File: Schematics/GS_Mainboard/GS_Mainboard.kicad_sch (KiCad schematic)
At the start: 0 parts

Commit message: Completed schematic
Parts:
- added C1: 10n, Capacitor_SMD:C_0603_1608Metric, symbol Device:C
- added C10, C32, C33, C5, C6, C9: 100n, Capacitor_SMD:C_0402_1005Metric, symbol Device:C
- added C11: 33pF, Capacitor_SMD:C_0402_1005Metric, symbol Device:C
- added C11 (x4): 47uF, Capacitor_SMD:C_0805_2012Metric, symbol Device:C
- added C11, C17: 22uF, Capacitor_SMD:C_0805_2012Metric, symbol Device:C
- added C11, C4 (x2), C7 (x2): 100nF, Capacitor_SMD:C_0603_1608Metric, symbol Device:C
- added C12: 10uF, Capacitor_SMD:C_0603_1608Metric, symbol Device:C
- added C13: 22uF, Capacitor_SMD:C_0603_1608Metric, symbol Device:C
- added C14: 2000uF, 25V, Capacitor_THT:CP_Radial_D12.5mm_P5.00mm, symbol Device:C_Polarized
- added C14: 1000uF, 25V, Capacitor_THT:CP_Radial_D10.0mm_P5.00mm, symbol Device:C_Polarized
- added C14: 100uF, Capacitor_SMD:CP_Elec_6.3x5.9, symbol Device:C_Polarized
- added C2 (x2): 2.2uF, Capacitor_SMD:C_0603_1608Metric_Pad1.08x0.95mm_HandSolder, symbol Device:C
- added C2 (x2): 4.7uF, Capacitor_SMD:C_0805_2012Metric, symbol Device:C
- added C2: 10uF, Capacitor_SMD:CP_Elec_4x5.4, symbol Device:C_Polarized
- added C29, C30, C34, C35, C36, C37, C38: 1uF, Capacitor_SMD:C_0603_1608Metric, symbol Device:C
- added C4, C8: 1uF, Capacitor_SMD:C_0805_2012Metric, symbol Device:C_Polarized
- added C46: 0.1u, Capacitor_SMD:C_0603_1608Metric, symbol Device:C
- added D1: DB_LED (YLW), LED_SMD:LED_0603_1608Metric, symbol Device:LED
- added D1: 12V PWR (GRN), LED_SMD:LED_0805_2012Metric, symbol Device:LED
- added D1: 5.0V PWR (GRN), LED_SMD:LED_0805_2012Metric, symbol Device:LED
- added D1: 3.3V PWR (GRN), LED_SMD:LED_0805_2012Metric, symbol Device:LED
- added D10, D11: 15Vz, Diode_SMD:D_SOD-123, symbol Device:D_Zener
- added D5, D6, D7, D8, D9: WS2812B, LED_SMD:LED_WS2812B_PLCC4_5.0x5.0mm_P3.2mm, symbol LED:WS2812B
- added FB1: 100R, Resistor_SMD:R_0805_2012Metric, symbol Device:FerriteBead
- added H1, H2, H3, H4, H5, H6: MountingHole, MountingHole:MountingHole_3.2mm_M3_ISO14580_Pad, symbol Mechanical:MountingHole
- added J1: SWD Header, footprints:PinHeader_1x6_P2.54mm_Drill1.02mm, symbol Connector:Conn_01x06_Pin
- added J10: GPIO, footprints:PinHeader_1x6_P2.54mm_Drill1.02mm, symbol Connector:Conn_01x06_Pin
- added J11: RTX_PWR, TerminalBlock:TerminalBlock_bornier-2_P5.08mm, symbol Connector:Screw_Terminal_01x02
- added J12: SRC_IND, TerminalBlock_TE-Connectivity:TerminalBlock_TE_282834-3_1x03_P2.54mm_Horizontal, symbol Connector:Screw_Terminal_01x03
- added J13: BATT1, TerminalBlock:TerminalBlock_bornier-2_P5.08mm, symbol Connector:Screw_Terminal_01x02
- added J14: BATT2, TerminalBlock:TerminalBlock_bornier-2_P5.08mm, symbol Connector:Screw_Terminal_01x02
- added J15: SWITCH, TerminalBlock:TerminalBlock_bornier-2_P5.08mm, symbol Connector:Screw_Terminal_01x02
- added J16: BUTTS, TerminalBlock:TerminalBlock_bornier-4_P5.08mm, symbol Connector:Screw_Terminal_01x04
- added J17: POWER, TerminalBlock:TerminalBlock_bornier-4_P5.08mm, symbol Connector:Screw_Terminal_01x04
- added J2: RASPI, footprints:PinHeader_1x6_P2.54mm_Drill1.02mm, symbol Connector:Conn_01x06_Pin
- added J3, J5: RGB_OUT, footprints:PinHeader_1x3_P2.54mm_Drill1.02mm, symbol dk_Rectangular-Connectors-Headers-Male-Pins:640456-3
- added J4: RGB_IN, footprints:PinHeader_1x3_P2.54mm_Drill1.02mm, symbol dk_Rectangular-Connectors-Headers-Male-Pins:640456-3
- added J6: FAN1, footprints:PinHeader_1x3_P2.54mm_Drill1.02mm, symbol dk_Rectangular-Connectors-Headers-Male-Pins:640456-3
- added J7: FAN2, footprints:PinHeader_1x3_P2.54mm_Drill1.02mm, symbol dk_Rectangular-Connectors-Headers-Male-Pins:640456-3
- added J8: RGB12V, TerminalBlock:TerminalBlock_bornier-4_P5.08mm, symbol Connector:Screw_Terminal_01x04
- added L2: 12uH, Inductor_SMD:L_Bourns_SRR1260, symbol Device:L
- added L2: 4.7uH, Inductor_SMD:L_Bourns_SRN8040TA, symbol Device:L
- added Q1 (x3): AO4447A, Package_SO:SOIC-8_3.9x4.9mm_P1.27mm, symbol Transistor_FET:IRF7404
- added Q1, Q10, Q11, Q2, Q3, Q4, Q5: AO3400A, Package_TO_SOT_SMD:SOT-23, symbol Transistor_FET:AO3400A
- added Q12, Q9: AO4406A, Package_SO:SOIC-8_3.9x4.9mm_P1.27mm, symbol Transistor_FET:IRF7403
- added R1, R17, R26, R35, R37, R38, R41, R44, R45, R46: 10k, Resistor_SMD:R_0603_1608Metric, symbol Device:R
- added R10, R7: 68k, Resistor_SMD:R_0603_1608Metric, symbol Device:R
- added R10: 33k, Resistor_SMD:R_0603_1608Metric, symbol Device:R
- added R10: 1k, Resistor_SMD:R_0603_1608Metric, symbol Device:R
- added R11: 6.2k, Resistor_SMD:R_0603_1608Metric, symbol Device:R
- added R11: 3.6k, Resistor_SMD:R_0603_1608Metric, symbol Device:R
- added R13, R14: 30k, Resistor_SMD:R_0603_1608Metric, symbol Device:R
- added R15: 47k, Resistor_SMD:R_0603_1608Metric, symbol Device:R
- added R16: 13k, Resistor_SMD:R_0603_1608Metric, symbol Device:R
- added R18, R2, R21, R23, R25, R29, R3, R40, R43: 100k, Resistor_SMD:R_0603_1608Metric, symbol Device:R
- added R19, R20, R22, R24, R27, R39, R42: 510R, Resistor_SMD:R_0603_1608Metric, symbol Device:R
- added R28: 100k, Resistor_SMD:R_0402_1005Metric, symbol Device:R
- added R30, R31: 1k, Resistor_THT:R_Axial_DIN0204_L3.6mm_D1.6mm_P5.08mm_Horizontal, symbol Device:R
- added R32, R33, R7: 15k, Resistor_SMD:R_0603_1608Metric, symbol Device:R
- added R34, R36: 75k, Resistor_SMD:R_0603_1608Metric, symbol Device:R
- added R4: 680R, Resistor_SMD:R_0603_1608Metric, symbol Device:R
- added R7: 3.3k, Resistor_SMD:R_0603_1608Metric, symbol Device:R
- added SW1: SW_STM_RESET, Button_Switch_SMD:SW_Push_1P1T_XKB_TS-1187A, symbol Switch:SW_Push
- added SW2: SW_STM_BOOT_MODE, Button_Switch_SMD:SW_Push_1P1T_XKB_TS-1187A, symbol Switch:SW_Push
- added TH1: 10k, Resistor_SMD:R_0603_1608Metric_Pad0.98x0.95mm_HandSolder, symbol Device:Thermistor_NTC
- added TP11: CURR, TestPoint:TestPoint_Pad_1.5x1.5mm, symbol Connector:TestPoint
- added TP5: 5VS, TestPoint:TestPoint_Pad_2.0x2.0mm, symbol Connector:TestPoint
- added TP5: 12VS, TestPoint:TestPoint_Pad_2.0x2.0mm, symbol Connector:TestPoint
- added TP5 (x2): B1_S, TestPoint:TestPoint_Pad_2.0x2.0mm, symbol Connector:TestPoint
- added U2: LMR51430XDDCR, Package_TO_SOT_SMD:SOT-23-6_Handsoldering, symbol QRET_Buck_PSU-symbols:LMR51430XDDCR
- added U3: K7805JT-500R3, footprints:K7805JT_500R3, symbol K7805JT_500R3:K7805JT-500R3
- added U4: 296-LMR51450FNDRRRCT-ND, footprints:LMR51450SDRRR, symbol LMR51450SDRRR:LMR51450SDRRR
- added U4: STM32F103C8T6, Package_QFP:LQFP-48_7x7mm_P0.5mm, symbol MCU_ST_STM32F1:STM32F103C8Tx
- added U5, U6: LM66100DCKR, footprints:LMR66100_SC-70-6, symbol QRET_Buck_PSU-symbols:LM66100DCKR
- added U7, U8: LM74700QDDFRQ1, footprints:LM74700_SOT-23-THIN_1P6X2P9_TEX-M, symbol LM74700QDDFRQ1:LM74700QDDFRQ1
- added U9: ACS37041KLHBLT-010B3, footprints:APS12628LLHALTBAP_HandSolder, symbol ACS37041KLHBLT-010B3:ACS37041KLHBLT-010B3
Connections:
- new net: D1.2 (A), R4.1
- new net: R10.2, R11.1, U2.4 (FB)
- new net: Q10.3 (D), R38.2, U7.1 (EN)
- new net: Q4.1 (G), R24.2
- new net: J8.2 (Pin_2), Q4.3 (D)
- new net: Q2.1 (G), R20.2
- new net: C11.1, R10.2
- new net: C11.2, R10.2, R11.1, U4.7 (FB)
- new net: J6.1, J7.1, Q1.3 (D)
- new net: C7.1, L2.1, U4.1 (SW), U4.2 (SW__1), U4.3 (SW__2)
- new net: C7.2, U4.4 (BOOT)
- new net: C7.1, L2.1, U2.2 (SW)
- new net: C7.2, U2.6 (CB)
- new net: J12.3 (Pin_3), R31.1
- new net: Q5.1 (G), R27.1
- new net: Q1.4 (G), Q5.3 (D), R28.2
- new net: D1.2 (A), R7.2 (x3)
- new net: J11.2 (Pin_2), Q1.5 (D), Q1.6 (D), Q1.7 (D), Q1.8 (D)
- new net: D10.2 (A), Q1.4 (G), R32.1
- new net: J13.2 (Pin_2), Q1.5 (D), Q1.6 (D), Q1.7 (D), Q1.8 (D)
- new net: D11.2 (A), Q1.4 (G), R33.1
- new net: D7.2 (DOUT), D8.4 (DIN)
- new net: D6.2 (DOUT), D7.4 (DIN)
- new net: Q1.1 (G), R19.2
- new net: Q10.1 (G), R39.2
- new net: J8.4 (Pin_4), Q2.3 (D)
- new net: C38.2, U8.4 (VCAP)
- new net: C35.2, U7.4 (VCAP)
- new net: Q9.4 (G), U7.6 (GATE)
- new net: Q12.4 (G), U8.6 (GATE)
- new net: J13.1 (Pin_1), J14.1 (Pin_1), J15.2 (Pin_2)
- new net: Q11.1 (G), R42.2
- new net: Q11.3 (D), R41.2, U8.1 (EN)
- new net: Q3.1 (G), R22.2
- new net: J14.2 (Pin_2), Q1.5 (D), Q1.6 (D), Q1.7 (D), Q1.8 (D)
- new net: J8.3 (Pin_3), Q3.3 (D)
- new net: C30.2, U6.2 (GND)
- new net: D8.2 (DOUT), D9.4 (DIN)
- new net: J12.2 (Pin_2), R30.1
- new net: D5.2 (DOUT), D6.4 (DIN)
- new net +12V: C11.1, C14.1, C17.1, J17.3 (Pin_3), J6.3, J7.3, J8.1 (Pin_1), L2.2, Q1.1 (S), Q1.2 (S), Q1.3 (S), R10.1, R15.2, R28.1
- new net +3.3V: C10.1, C11.1, C2.1, C5.1, C6.1, C8.1, C9.1, FB1.2, J10.2 (Pin_2), J3.2, R1.2, R17.2, R26.1, R44.2, R45.2, R46.2, R7.1, R7.1, R7.1, SW2.2, U4.1 (VBAT), U4.24 (VDD), U4.36 (VDD), U4.48 (VDD), U5.3 (*CE), U5.6 (VOUT), U6.3 (*CE), U6.6 (VOUT)
- new net +3.3VA: C1.1, C4.1, FB1.1, U4.9 (VDDA)
- new net +5V: C11.1, C11.1, C14.1, J17.4 (Pin_4), J2.1 (Pin_1), J2.2 (Pin_2), L2.2, R10.1, R10.1, R13.2
- new net +BATT: C11.1, C12.1, C14.1, C2.1, C2.1, C4.1, C4.1, J17.2 (Pin_2), U2.3 (VIN), U2.5 (EN), U3.1 (+Vin), U4.10 (VIN), U4.11 (VIN__1), U4.12 (VIN__2), U4.9 (EN), U9.2 (IP-)
- new net 12V_SENSE: R15.1, R16.2, TP5.1, U4.14 (PA4)
- new net 5V_SENSE: R13.1, R14.2, TP5.1, U4.13 (PA3)
- new net BATT1_EN: R30.2, R39.1, R40.2, U4.17 (PA7)
- new net BATT1_RAW: C35.1, C36.1, D10.1 (K), Q1.1 (S), Q1.2 (S), Q1.3 (S), Q9.1 (S), Q9.2 (S), Q9.3 (S), R34.1, R38.1, U7.5 (ANODE)
- new net BATT2_EN: R31.2, R42.1, R43.2, U4.29 (PA8)
- new net BATT2_RAW: C37.1, C38.1, D11.1 (K), Q1.1 (S), Q1.2 (S), Q1.3 (S), Q12.1 (S), Q12.2 (S), Q12.3 (S), R36.1, R41.1, U8.5 (ANODE)
- new net BATT_1_SENSE: C32.1, R34.2, R35.1, TP5.1, U4.10 (PA0)
- new net BATT_2_SENSE: C33.1, R36.2, R37.1, TP5.1, U4.11 (PA1)
- new net BATT_COM: C34.1, Q12.5 (D), Q12.6 (D), Q12.7 (D), Q12.8 (D), Q9.5 (D), Q9.6 (D), Q9.7 (D), Q9.8 (D), U7.8 (CATHODE), U8.8 (CATHODE), U9.1 (IP+)
- new net BOOT0: R2.2, SW2.1, U4.44 (BOOT0)
- new net BOOT1: R3.2, U4.20 (PB2)
- new net BUTT_1: J16.2 (Pin_2), R44.1, U4.46 (PB9)
- new net BUTT_2: J16.3 (Pin_3), R45.1, U4.43 (PB7)
- new net BUTT_3: J16.4 (Pin_4), R46.1, U4.45 (PB8)
- new net CURR_PWR: C46.1, U4.16 (PA6), U9.5 (VDD)
- new net CURR_SENSE: TP11.1, U4.12 (PA2), U9.4 (VOUT)
- new net DB_LED: R4.2, U4.38 (PA15)
- new net FAN_PWM: R18.2, R19.1, U4.19 (PB1)
- new net FAN_TACH: J6.2, R17.1, U4.18 (PB0)
- new net GND: C1.2, C10.2, C11.2, C11.2, C11.2, C11.2, C11.2, C11.2, C12.2, C13.2, C14.2, C14.2, C17.2, C2.2, C2.2, C2.2, C29.2, C32.2, C33.2, C34.2, C36.2, C37.2, C4.2, C4.2, C4.2, C5.2, C6.2, C8.2, C9.2, D1.1 (K), D1.1 (K), D1.1 (K), D1.1 (K), J1.1 (Pin_1), J10.1 (Pin_1), J11.1 (Pin_1), J12.1 (Pin_1), J15.1 (Pin_1), J16.1 (Pin_1), J17.1 (Pin_1), J2.3 (Pin_3), J2.4 (Pin_4), J3.1, Q1.2 (S), Q10.2 (S), Q11.2 (S), Q2.2 (S), Q3.2 (S), Q4.2 (S), Q5.2 (S), R11.2, R11.2, R14.1, R16.1, R18.1, R2.1, R21.1, R23.1, R25.1, R29.1, R3.1, R32.2, R33.2, R35.2, R37.2, R40.1, R43.1, SW1.1, TH1.2, U2.1 (GND), U3.4 (GND), U4.13 (PGND), U4.23 (VSS), U4.35 (VSS), U4.47 (VSS), U4.8 (AGND), U4.8 (VSSA), U5.2 (GND), U5.5 (ST), U6.5 (ST), U7.2 (GND), U8.2 (GND)
- new net GND2: C14.2, C46.2, U9.3 (GND)
- new net GPIO1: J10.4 (Pin_4), U4.25 (PB12)
- new net GPIO2: J10.3 (Pin_3), U4.26 (PB13)
- new net OSC_IN: U4.5 (PD0)
- new net OSC_OUT: U4.6 (PD1)
- new net PSU_TEMP: R26.2, TH1.1, U4.15 (PA5)
- new net RGB12_B: R22.1, R23.2, U4.41 (PB5)
- new net RGB12_G: R20.1, R21.2, U4.40 (PB4)
- new net RGB12_R: R24.1, R25.2, U4.39 (PB3)
- new net RGB_DATA: J3.3, U4.27 (PB14)
- new net RGB_DATA_IN: D5.4 (DIN), J4.3
- new net RGB_DATA_OUT: D9.2 (DOUT), J5.3
- new net RGB_GND: C2.1, C2.1, D5.3 (VSS), D6.3 (VSS), D7.3 (VSS), D8.3 (VSS), D9.3 (VSS), J4.1, J5.1
- new net RGB_V+: C2.2, C2.2, D5.1 (VDD), D6.1 (VDD), D7.1 (VDD), D8.1 (VDD), D9.1 (VDD), J4.2, J5.2
- new net RX: J1.5 (Pin_5), J2.5 (Pin_5), U4.31 (PA10)
- new net SCL: J10.6 (Pin_6), U4.21 (PB10)
- new net SDA: J10.5 (Pin_5), U4.22 (PB11)
- new net STM_RESET: C11.1, R1.1, SW1.2, U4.7 (NRST)
- new net SWCLK: J1.4 (Pin_4), U4.37 (PA14)
- new net SWDIO: J1.3 (Pin_3), U4.34 (PA13)
- new net TX: J1.6 (Pin_6), J2.6 (Pin_6), U4.30 (PA9)
- new net VRX_PWR: R27.2, R29.2, U4.28 (PB15)
- new net V_BUCK: C13.1, C29.1, U3.3 (NC), U5.1 (VIN)
- new net V_SWD: C30.1, J1.2 (Pin_2), U6.1 (VIN)
- no-connect marks 0 -> 9
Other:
- note added: "12V Buck Power Supply (3A)"
- note added: "12V RGB Control"
- note added: "28V MAX"
- note added: "3.3V Buck Power Supply (500mA)"
- note added: "5V Buck Power Supply (5A)"
- note added: "ADC"
- note added: "Additional Filtering for Analogue VDD"
- note added: "B0 HIGH = PROGRAMMING MODE B0 LOW = RUN MEMORY"
- note added: "Battery Current Sensor"
- note added: "Battery Frontend (RPP)"
- note added: "Battery Selection Control & RCB"
- note added: "Battery Source Indicator LEDs"
- note added: "Battery Voltage Sensors"
- note added: "Button Inputs"
- note added: "Camera VRX Power Control"
- note added: "Debug LED"
- note added: "FOLLOW LAYOUT EXAMPLE (9.4.2) FROM DATASHEET LMR51430: PFM @ 500kHz (simpler routing & higher efficiency)"
- note added: "FOLLOW LAYOUT EXAMPLE (9.5.2) FROM DATASHEET LMR51450: FPFM @ 500kHz (lower efficiency but more stable)"
- note added: "Fan Control"
- note added: "GENERIC"
- note added: "Good for ~1A"
- note added: "Good for ~1A per CH"
- note added: "I2C"
- note added: "INT"
- note added: "Ideal Diodes (Input MUX + RPP)"
- note added: "Ignoring PG"
- note added: "Max Output: 3.0A"
- note added: "Max Output: 5.0A"
- note added: "Max: 15.2V"
- note added: "Max: 6.6V"
- note added: "Mounting Holes"
- note added: "One 100nf "high quality ceramic" capacitor for each VDD and VBAT One 10uf electrolytic capacitor for bulk filtering. Place them as close as possible to the IC - one cap per input pin"
- note added: "PIN HEADERS"
- note added: "POWER OUTPUT"
- note added: "PSU Temp Sensor"
- note added: "PWM"
- note added: "Power LEDs"
- note added: "RGB Indicator Board (SEPARATE PCB)"
- note added: "RT Open = 500kHz"
- note added: "Rfbt=33k, Rfbb=6.2k, Vref=0.8V Vout = ((Rfbt*0.8)/Rfbb)+0.8 Vout = 5.058V"
- note added: "Rfbt=68k, Rfbb=3.6k, Vref=0.6V Vout = ((Rfbt*0.6)/Rfbb)+0.6 Vout = 11.933V"
- note added: "STM32 Boot Mode"
- note added: "STM32 Decoupling Capacitors for VBAT and VDD"
- note added: "STM32 Reset"
- note added: "Serial Wire Debug + USART"
- note added: "TO RASPI"
- note added: "TO RGB PCB"
- note added: "USART"
- note added: "Vf=2.1V, I=1.8mA, R=680"
- note added: "Vin=12V, Vf=2.8V, R=0.14mA, R=68k"
- note added: "Vin=3.3V, Vf=2.8V, R=0.15mA, R=3.3k"
- note added: "Vin=5.0V, Vf=2.8V, R=0.15mA, R=15k"
- note added: "Voltage Rail Sensing"
- note added: "Zeners to clamp V(gs) to <15V"

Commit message: Several schematic improvements
- Removed initial redundant reverse-polarity-protection and added clamping diodes for affected ADC inputs (should reduce cost & part count)
- Updated contributor list
- Added missing part numbers
- Added switched 12V AUX output
- Added lid sensor input
- Changed some connectors to be smaller
- Reworked exposed GPIO pins
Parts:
- removed D10, D11: 15Vz, Diode_SMD:D_SOD-123, symbol Device:D_Zener
- removed J16: BUTTS, TerminalBlock:TerminalBlock_bornier-4_P5.08mm, symbol Connector:Screw_Terminal_01x04
- removed Q1 (x2): AO4447A, Package_SO:SOIC-8_3.9x4.9mm_P1.27mm, symbol Transistor_FET:IRF7404
- removed R32, R33: 15k, Resistor_SMD:R_0603_1608Metric, symbol Device:R
- added D10, D11: SS54, Diode_SMD:D_SMA, symbol Device:D_Schottky
- added J16: BUTTS, footprints:PinHeader_1x6_P2.54mm_Drill1.02mm, symbol Connector:Conn_01x06_Pin
- added J9: RTX_PWR, TerminalBlock:TerminalBlock_bornier-2_P5.08mm, symbol Connector:Screw_Terminal_01x02
- added Q1: AO4447A, Package_SO:SOIC-8_3.9x4.9mm_P1.27mm, symbol Transistor_FET:IRF7404
- added Q7: AO3400A, Package_TO_SOT_SMD:SOT-23, symbol Transistor_FET:AO3400A
- added R47: 100k, Resistor_SMD:R_0603_1608Metric, symbol Device:R
- added R48: 510R, Resistor_SMD:R_0603_1608Metric, symbol Device:R
- added R49: 100k, Resistor_SMD:R_0402_1005Metric, symbol Device:R
- added R50: 10k, Resistor_SMD:R_0603_1608Metric, symbol Device:R
- J11: value RTX_PWR -> AUX_PWR; Digikey (none) -> 5239-ELK508V-02P-ND
- J13, J14, J15: Digikey (none) -> 5239-ELK508V-02P-ND
- J4, J5: now left out of the parts list
- Q1: Type (none) -> P-CH
- Q5: Type (none) -> N-CH
- R4: footprint Resistor_SMD:R_0603_1608Metric -> Resistor_SMD:R_0805_2012Metric; JLCPCB C23228 -> C2296
- TP5: value B1_S -> B2_S
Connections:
- net +12V: now also Q1.1 (S), Q1.2 (S), Q1.3 (S), R49.1
- net +3.3V: now also R50.2
- net BATT1_RAW: now also J13.2 (Pin_2)
- net BATT2_RAW: now also J14.2 (Pin_2)
- net BATT_1_SENSE: now also D10.1 (K)
- net BATT_2_SENSE: now also D11.1 (K)
- net BUTT_1: now also J16.2 (Pin_2)
- net BUTT_2: now also J16.3 (Pin_3)
- net BUTT_3: now also J16.4 (Pin_4)
- net FAN_PWM: now also U4.32 (PA11); no longer U4.19 (PB1)
- net FAN_TACH: now also U4.33 (PA12); no longer U4.18 (PB0)
- net GND: now also D10.2 (A), D11.2 (A), J16.1 (Pin_1), J16.5 (Pin_5), J9.1 (Pin_1), Q7.2 (S), R47.1
- net GPIO1: now also U4.18 (PB0); no longer U4.25 (PB12)
- net GPIO2: now also U4.19 (PB1); no longer U4.26 (PB13)
- net at Q1.5 (D), Q1.6 (D), Q1.7 (D)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: now also J9.2 (Pin_2); no longer J11.2 (Pin_2)
- net LID_SENSE: now reaches U4.42 (PB6)
- net LID_SENSE: now also J16.6 (Pin_6), R50.1
- net OSC_IN: no longer names the net of U4.5 (PD0)
- net OSC_OUT: no longer names the net of U4.6 (PD1)
- new net: Q7.1 (G), R48.1
- new net: J11.2 (Pin_2), Q1.5 (D), Q1.6 (D), Q1.7 (D), Q1.8 (D)
- new net: Q1.4 (G), Q7.3 (D), R49.2
- new net AUX_PWR: R47.2, R48.2, U4.26 (PB13)
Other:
- note added: "AUX 12V Power Control"
- note added: "Battery + Switch Connections"
- note added: "Battery Selection Control, RPP, & RCB"
- note added: "Button Inputs + Lid Sensor"
- note added: "OSC"
- note added: "SS54 to clamp negative voltage"
- note removed: "Battery Frontend (RPP)"
- note removed: "Battery Selection Control & RCB"
- note removed: "Button Inputs"
- note removed: "Zeners to clamp V(gs) to <15V"
- moved on the sheet: C32, C33, D1, J11, J12, J13, J14, J15, J17, Q1, Q5, R27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

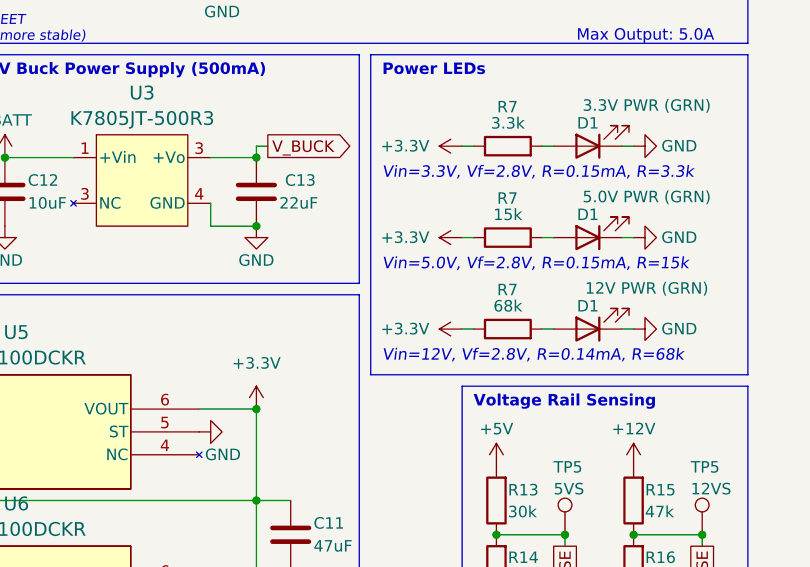
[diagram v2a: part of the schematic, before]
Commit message: Fixed power LED voltage sources
5V and 12V LEDs were connected to 3.3V. Thanks Teighin :)
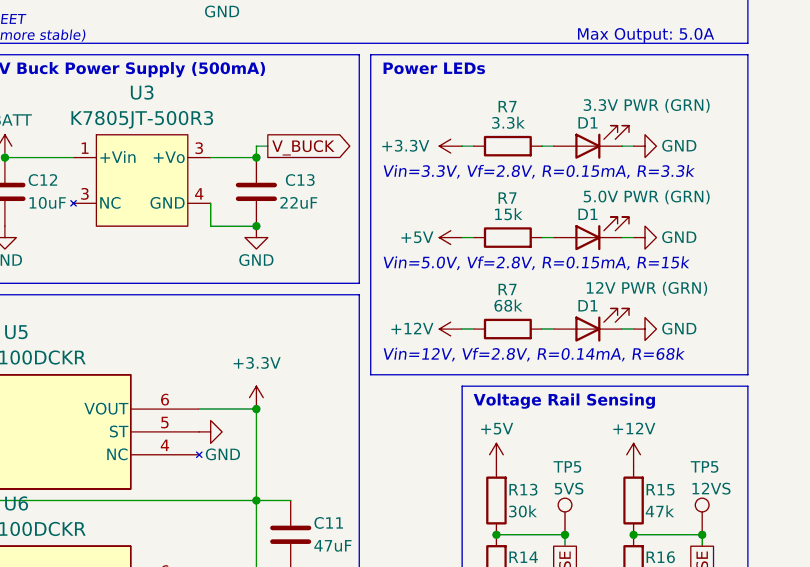
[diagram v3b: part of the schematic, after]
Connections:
- net +12V: now also R7.1
- net +3.3V: no longer R7.1, R7.1
- net +5V: now also R7.1
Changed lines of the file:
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@@
     )
   )
+  (symbol (lib_id "power:+5V") (at 374.65 118.11 90) (unit 1)
+    (in_bom yes) (on_board yes) (dnp no) (fields_autoplaced)
+    (property "Reference" "#PWR034" (at 378.46 118.11 0)
+      (effects (font (size 1.27 1.27)) hide)
+    )
+    (property "Value" "+5V" (at 371.4751 118.11 90)
+      (effects (font (size 1.27 1.27)) (justify left))
+    )
+    (property "Footprint" "" (at 374.65 118.11 0)
+      (effects (font (size 1.27 1.27)) hide)
+    )
+    (property "Datasheet" "" (at 374.65 118.11 0)
+      (effects (font (size 1.27 1.27)) hide)
+    )
+    (pin "1")
+    (instances
+      (project "GS_Mainboard"
+        (path "/235e6551-f8bc-42ed-8277-1e6d1d06a12a"
+          (reference "#PWR034") (unit 1)
+        )
+      )
+    )
+  )
   (symbol (lib_id "Device:L") (at 359.41 27.94 90) (unit 1)
     (in_bom yes) (on_board yes) (dnp no) (fields_autoplaced)
@@
     )
   )
-  (symbol (lib_id "power:+3.3V") (at 374.65 128.27 90) (unit 1)
-    (in_bom yes) (on_board yes) (dnp no)
-    (property "Reference" "#PWR036" (at 378.46 128.27 0)
-      (effects (font (size 1.27 1.27)) hide)
-    )
-    (property "Value" "+3.3V" (at 368.3 128.27 90)
-      (effects (font (size 1.27 1.27)))
-    )
-    (property "Footprint" "" (at 374.65 128.27 0)
-      (effects (font (size 1.27 1.27)) hide)
-    )
-    (property "Datasheet" "" (at 374.65 128.27 0)
-      (effects (font (size 1.27 1.27)) hide)
-    )
-    (pin "1")
-    (instances
-      (project "GS_Mainboard"
-        (path "/235e6551-f8bc-42ed-8277-1e6d1d06a12a"
-          (reference "#PWR036") (unit 1)
-        )
-      )
-      (project "Altimeter_Module"
-        (path "/29db4100-776d-46b8-a17b-170206e82f23"
-          (reference "#PWR016") (unit 1)
-        )
-      )
-      (project "Communications_Module"
-        (path "/ace06731-9b48-45c3-868d-c65fed1a8f9b"
-          (reference "#PWR022") (unit 1)
-        )
-      )
-      (project "processor"
-        (path "/ccfbe2af-01d0-4f8a-8e0b-98df5d6602a9"
-          (reference "#PWR?") (unit 1)
-        )
-      )
-    )
-  )
   (symbol (lib_id "power:GND") (at 345.44 158.75 90) (unit 1)
     (in_bom yes) (on_board yes) (dnp no)
@@
     )
   )
+  (symbol (lib_id "power:+12V") (at 374.65 128.27 90) (unit 1)
+    (in_bom yes) (on_board yes) (dnp no) (fields_autoplaced)
+    (property "Reference" "#PWR036" (at 378.46 128.27 0)
+      (effects (font (size 1.27 1.27)) hide)
+    )
+    (property "Value" "+12V" (at 371.475 128.27 90)
+      (effects (font (size 1.27 1.27)) (justify left))
+    )
+    (property "Footprint" "" (at 374.65 128.27 0)
+      (effects (font (size 1.27 1.27)) hide)
+    )
+    (property "Datasheet" "" (at 374.65 128.27 0)
+      (effects (font (size 1.27 1.27)) hide)
+    )
+    (pin "1")
+    (instances
+      (project "GS_Mainboard"
+        (path "/235e6551-f8bc-42ed-8277-1e6d1d06a12a"
+          (reference "#PWR036") (unit 1)
+        )
+      )
+    )
+  )
   (symbol (lib_id "Device:C") (at 26.67 213.36 0) (unit 1)
     (in_bom yes) (on_board yes) (dnp no)
@@
         )
       )
-    )
-  )
-  (symbol (lib_id "power:+3.3V") (at 374.65 118.11 90) (unit 1)
-    (in_bom yes) (on_board yes) (dnp no)
-    (property "Reference" "#PWR034" (at 378.46 118.11 0)
-      (effects (font (size 1.27 1.27)) hide)
-    )
-    (property "Value" "+3.3V" (at 368.3 118.11 90)
-      (effects (font (size 1.27 1.27)))
-    )
-    (property "Footprint" "" (at 374.65 118.11 0)
-      (effects (font (size 1.27 1.27)) hide)
-    )
-    (property "Datasheet" "" (at 374.65 118.11 0)
-      (effects (font (size 1.27 1.27)) hide)
-    )
-    (pin "1")
-    (instances
-      (project "GS_Mainboard"
-        (path "/235e6551-f8bc-42ed-8277-1e6d1d06a12a"
-          (reference "#PWR034") (unit 1)
-        )
-      )
-      (project "Altimeter_Module"
-        (path "/29db4100-776d-46b8-a17b-170206e82f23"
-          (reference "#PWR016") (unit 1)
-        )
-      )
-      (project "Communications_Module"
-        (path "/ace06731-9b48-45c3-868d-c65fed1a8f9b"
-          (reference "#PWR022") (unit 1)
-        )
-      )
-      (project "processor"
-        (path "/ccfbe2af-01d0-4f8a-8e0b-98df5d6602a9"
-          (reference "#PWR?") (unit 1)
-        )
-      )

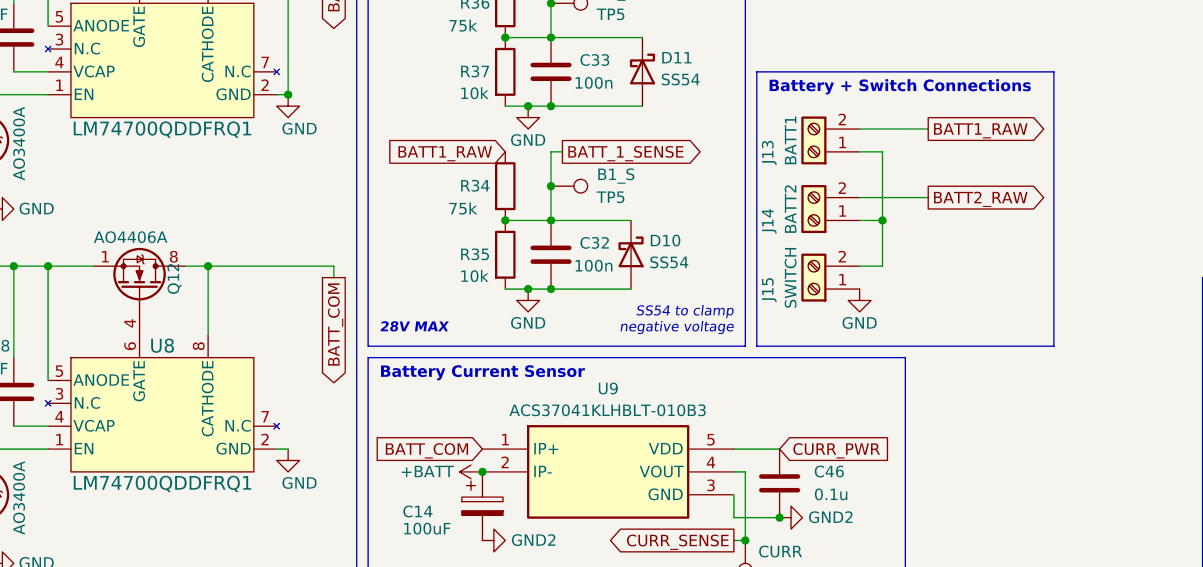
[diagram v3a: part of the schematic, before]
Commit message: Added ATC fuse
Also fixed wrong part number
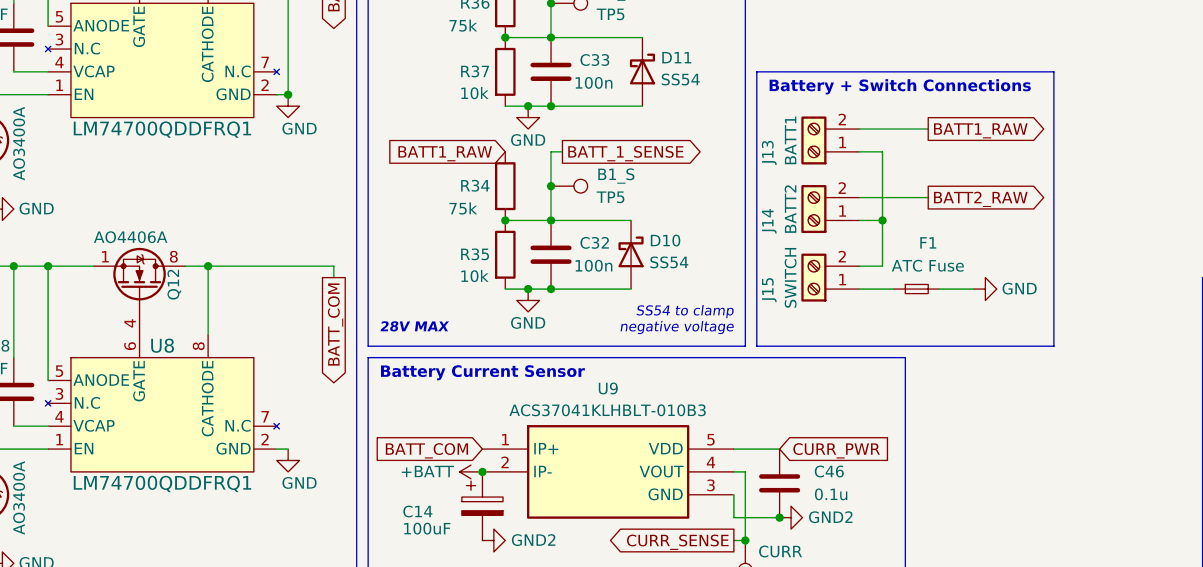
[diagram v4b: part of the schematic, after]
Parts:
- added F1: ATC Fuse, Fuse:Fuseholder_Keystone_3555-2, symbol Device:Fuse_Small
- D1: footprint LED_SMD:LED_0603_1608Metric -> LED_SMD:LED_0805_2012Metric; JLCPCB C72038 -> C2296
- R4: footprint Resistor_SMD:R_0805_2012Metric -> Resistor_SMD:R_0603_1608Metric; JLCPCB C2296 -> C23228
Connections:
- net GND: now also F1.2; no longer J15.1 (Pin_1)
- new net: F1.1, J15.1 (Pin_1)
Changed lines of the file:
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@@
     (stroke (width 0) (type default))
   )
+  (wire (pts (xy 138.43 250.19) (xy 142.24 250.19))
+    (stroke (width 0) (type default))
+  )
   (wire (pts (xy 295.91 22.86) (xy 307.34 22.86))
     (stroke (width 0) (type default))
@@
     (stroke (width 0) (type default))
   )
+  (wire (pts (xy 129.54 250.19) (xy 133.35 250.19))
+    (stroke (width 0) (type default))
+  )
   (wire (pts (xy 219.71 262.89) (xy 224.79 262.89))
     (stroke (width 0) (type default))
@@
       (effects (font (size 1.27 1.27)))
     )
-    (property "Footprint" "LED_SMD:LED_0603_1608Metric" (at 203.2 58.42 0)
+    (property "Footprint" "LED_SMD:LED_0805_2012Metric" (at 203.2 58.42 0)
       (effects (font (size 1.27 1.27)) hide)
     )
@@
       (effects (font (size 1.27 1.27)) hide)
     )
-    (property "JLCPCB" "C72038" (at 203.2 58.42 0)
+    (property "JLCPCB" "C2296" (at 203.2 58.42 0)
       (effects (font (size 1.27 1.27)) hide)
     )
@@
     )
   )
+  (symbol (lib_id "Device:Fuse_Small") (at 135.89 250.19 0) (unit 1)
+    (in_bom yes) (on_board yes) (dnp no)
+    (property "Reference" "F1" (at 137.16 245.11 0)
+      (effects (font (size 1.27 1.27)))
+    )
+    (property "Value" "ATC Fuse" (at 137.16 247.65 0)
+      (effects (font (size 1.27 1.27)))
+    )
+    (property "Footprint" "Fuse:Fuseholder_Keystone_3555-2" (at 135.89 250.19 0)
+      (effects (font (size 1.27 1.27)) hide)
+    )
+    (property "Datasheet" "~" (at 135.89 250.19 0)
+      (effects (font (size 1.27 1.27)) hide)
+    )
+    (property "Digikey" "36-3522-2-ND" (at 135.89 250.19 0)
+      (effects (font (size 1.27 1.27)) hide)
+    )
+    (pin "1")
+    (pin "2")
+    (instances
+      (project "GS_Mainboard"
+        (path "/235e6551-f8bc-42ed-8277-1e6d1d06a12a"
+          (reference "F1") (unit 1)
+        )
+      )
+    )
+  )
   (symbol (lib_id "dk_Rectangular-Connectors-Headers-Male-Pins:640456-3") (at 393.7 228.6 90) (unit 1)
     (in_bom yes) (on_board yes) (dnp no) (fields_autoplaced)
@@
     )
   )
-  (symbol (lib_id "power:GND") (at 129.54 250.19 0) (unit 1)
+  (symbol (lib_id "power:GND") (at 142.24 250.19 90) (unit 1)
     (in_bom yes) (on_board yes) (dnp no)
-    (property "Reference" "#PWR072" (at 129.54 256.54 0)
+    (property "Reference" "#PWR072" (at 148.59 250.19 0)
       (effects (font (size 1.27 1.27)) hide)
     )
-    (property "Value" "GND" (at 129.54 254 0)
+    (property "Value" "GND" (at 147.32 250.19 90)
       (effects (font (size 1.27 1.27)))
     )
-    (property "Footprint" "" (at 129.54 250.19 0)
+    (property "Footprint" "" (at 142.24 250.19 0)
       (effects (font (size 1.27 1.27)) hide)
     )
-    (property "Datasheet" "" (at 129.54 250.19 0)
+    (property "Datasheet" "" (at 142.24 250.19 0)
       (effects (font (size 1.27 1.27)) hide)
     )
@@
       (effects (font (size 1.27 1.27)))
     )
-    (property "Footprint" "Resistor_SMD:R_0805_2012Metric" (at 193.04 56.642 90)
+    (property "Footprint" "Resistor_SMD:R_0603_1608Metric" (at 193.04 56.642 90)
       (effects (font (size 1.27 1.27)) hide)
     )
@@
       (effects (font (size 1.27 1.27)) hide)
     )
-    (property "JLCPCB" "C2296" (at 193.04 58.42 0)
-      (effects (font (size 1.27 1.27)) hide)
-    )
-    (property "Field5" "" (at 193.04 58.42 90)
+    (property "JLCPCB" "C23228" (at 193.04 58.42 0)
       (effects (font (size 1.27 1.27)) hide)
     )
@@
   (symbol (lib_id "Transistor_FET:IRF7403") (at 49.53 250.19 270) (mirror x) (unit 1)
     (in_bom yes) (on_board yes) (dnp no)
-    (property "Reference" "Q12" (at 53.34 250.825 0)
+    (property "Reference" "Q12" (at 53.34 251.46 0)
       (effects (font (size 1.27 1.27)) (justify left))
     )
